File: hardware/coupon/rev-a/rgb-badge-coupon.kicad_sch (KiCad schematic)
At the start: 0 parts

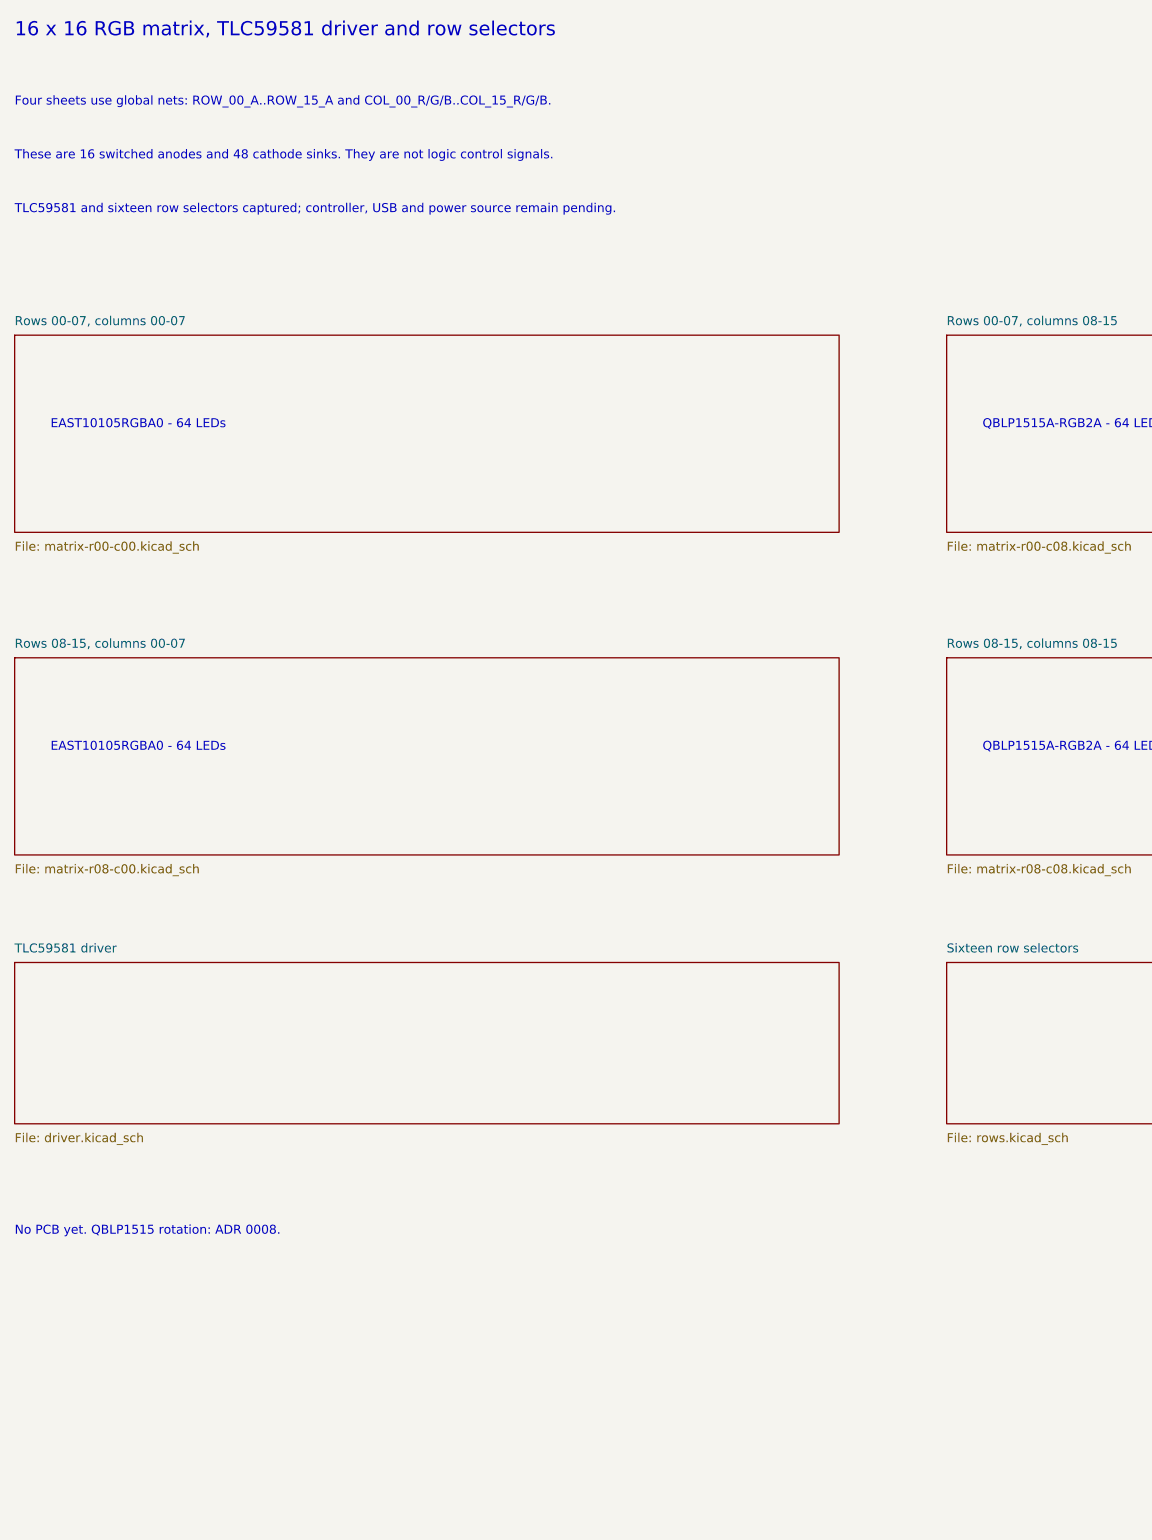
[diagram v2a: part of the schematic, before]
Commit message: Capture Coupon Rev A ESP32-S3 controller
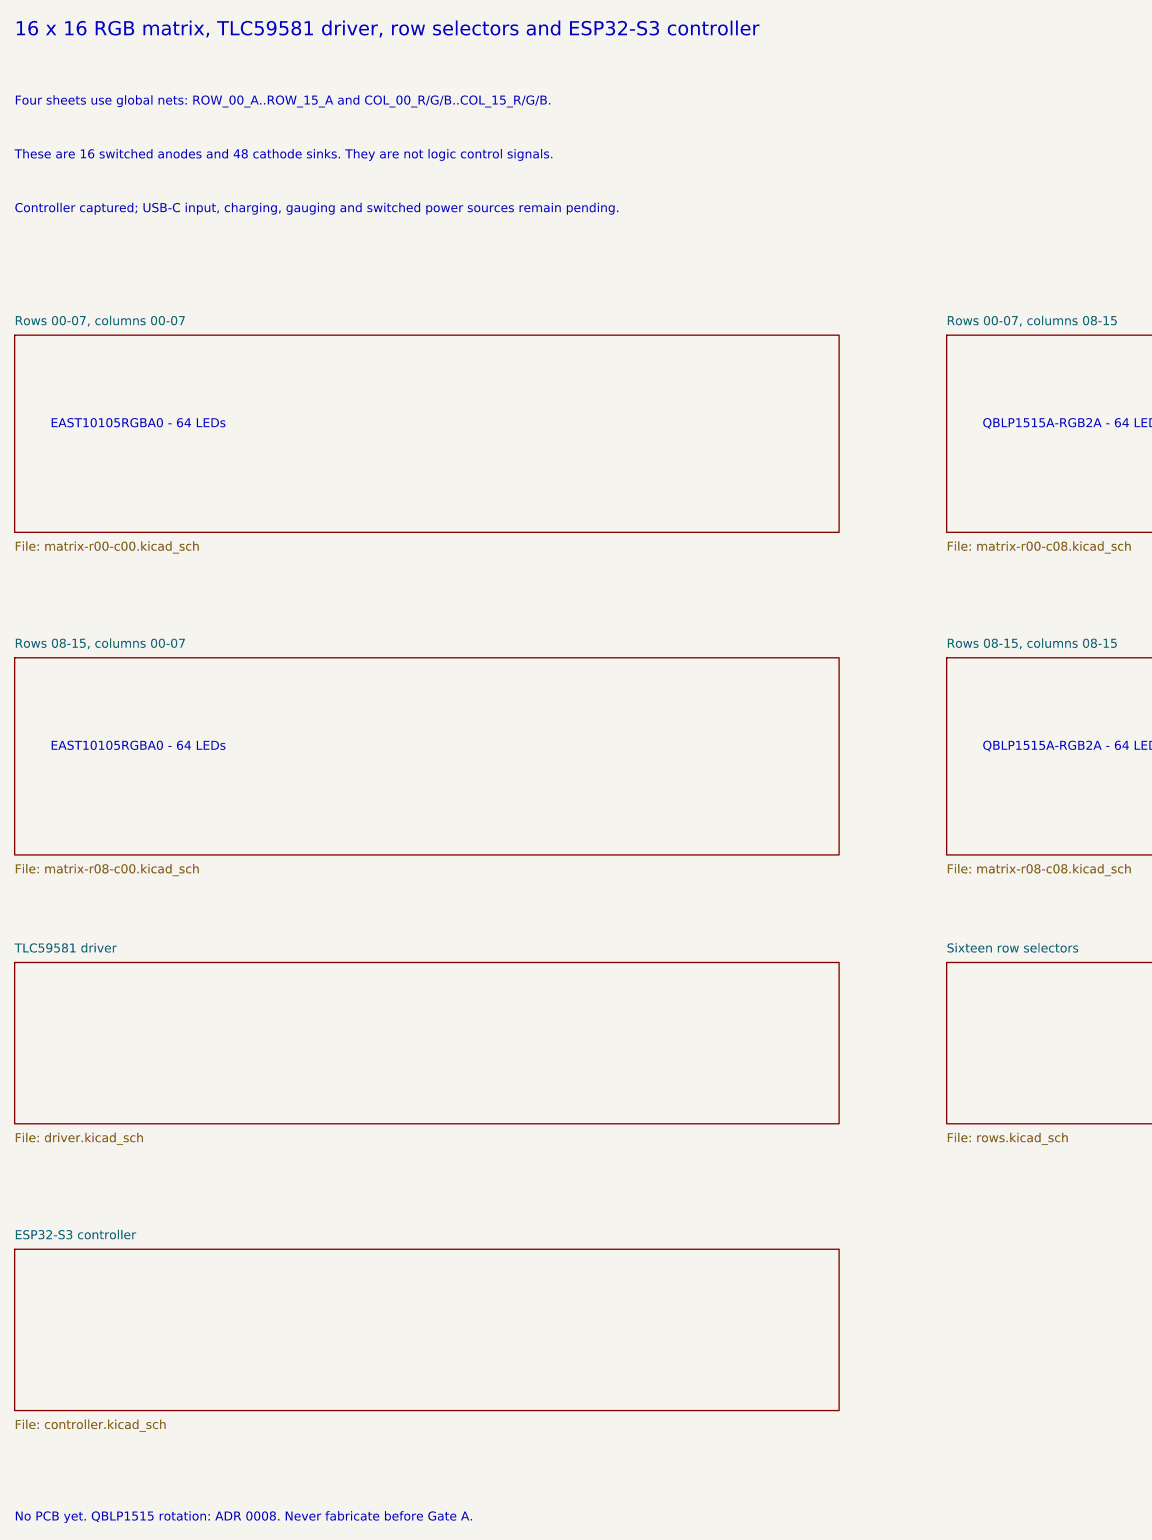
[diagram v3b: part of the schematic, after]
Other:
- added sheet ESP32-S3 controller (controller.kicad_sch)
- note added: "16 x 16 RGB matrix, TLC59581 driver, row selectors and ESP32-S3 controller"
- note added: "Controller captured; USB-C input, charging, gauging and switched power sources remain pending."
- note added: "No PCB yet. QBLP1515 rotation: ADR 0008. Never fabricate before Gate A."
- note removed: "16 x 16 RGB matrix, TLC59581 driver and row selectors"
- note removed: "No PCB yet. QBLP1515 rotation: ADR 0008."
- note removed: "TLC59581 and sixteen row selectors captured; controller, USB and power source remain pending."
- title: Coupon Rev A - matrix, driver and rows -> Coupon Rev A - matrix, driver, rows and controller
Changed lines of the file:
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@@
 (generator "rgb_badge_matrix")
 (generator_version "1.0")
-(paper "A4")
-(title_block (title "Coupon Rev A - matrix, driver and rows") (rev "A-draft") (comment 1 "SPDX-License-Identifier: CERN-OHL-S-2.0") (comment 2 "Controller and power circuits pending"))
-(text "16 x 16 RGB matrix, TLC59581 driver and row selectors" (at 20.32 20.32 0) (effects (font (size 2.0 2.0)) (justify left)))
+(paper "A3")
+(title_block (title "Coupon Rev A - matrix, driver, rows and controller") (rev "A-draft") (comment 1 "SPDX-License-Identifier: CERN-OHL-S-2.0") (comment 2 "USB-C input, charging and switched power circuits pending"))
+(text "16 x 16 RGB matrix, TLC59581 driver, row selectors and ESP32-S3 controller" (at 20.32 20.32 0) (effects (font (size 2.0 2.0)) (justify left)))
 (text "Four sheets use global nets: ROW_00_A..ROW_15_A and COL_00_R/G/B..COL_15_R/G/B." (at 20.32 30.48 0) (effects (font (size 1.27 1.27)) (justify left)))
 (text "These are 16 switched anodes and 48 cathode sinks. They are not logic control signals." (at 20.32 38.10 0) (effects (font (size 1.27 1.27)) (justify left)))
-(text "TLC59581 and sixteen row selectors captured; controller, USB and power source remain pending." (at 20.32 45.72 0) (effects (font (size 1.27 1.27)) (justify left)))
-(text "No PCB yet. QBLP1515 rotation: ADR 0008." (at 20.32 190.50 0) (effects (font (size 1.27 1.27)) (justify left)))
+(text "Controller captured; USB-C input, charging, gauging and switched power sources remain pending." (at 20.32 45.72 0) (effects (font (size 1.27 1.27)) (justify left)))
+(text "No PCB yet. QBLP1515 rotation: ADR 0008. Never fabricate before Gate A." (at 20.32 231.14 0) (effects (font (size 1.27 1.27)) (justify left)))
 (sheet (at 20.32 63.50) (size 116.84 27.94)
 (exclude_from_sim no) (in_bom yes) (on_board yes) (dnp no)
@@
 (property "Sheetfile" "rows.kicad_sch" (at 152.40 176.53 0) (effects (font (size 1.27 1.27)) (justify left top)))
 (instances (project "rgb-badge-coupon" (path "/207fb68e-2ddb-46bb-8712-eba2f8c5eef6" (page "7")))))
+(sheet (at 20.32 193.04) (size 116.84 22.86)
+(exclude_from_sim no) (in_bom yes) (on_board yes) (dnp no)
+(stroke (width 0.1524) (type solid)) (fill (color 0 0 0 0))
+(property "Sheetname" "ESP32-S3 controller" (at 20.32 191.77 0) (effects (font (size 1.27 1.27)) (justify left bottom)))
+(property "Sheetfile" "controller.kicad_sch" (at 20.32 217.17 0) (effects (font (size 1.27 1.27)) (justify left top)))
+(instances (project "rgb-badge-coupon" (path "/207fb68e-2ddb-46bb-8712-eba2f8c5eef6" (page "8")))))
 (sheet_instances (path "/" (page "1")))
 (embedded_fonts no)

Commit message: Capture conditioned USB permission gates and verify their actual wiring
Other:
- added sheet USB input conditioning (staged) (usb-conditioning.kicad_sch)
- added sheet USB permission gates (staged) (usb-permission.kicad_sch)
- note added: "USB logic captured with test boundaries; detectors, startup inhibition, charging and rail sources remain pending."
- note removed: "Controller captured; USB-C input, charging, gauging and switched power sources remain pending."
- title: Coupon Rev A - matrix, driver, rows and controller -> Coupon Rev A - display, controller and staged USB logic
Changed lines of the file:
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@@
 (generator_version "1.0")
 (paper "A3")
-(title_block (title "Coupon Rev A - matrix, driver, rows and controller") (rev "A-draft") (comment 1 "SPDX-License-Identifier: CERN-OHL-S-2.0") (comment 2 "USB-C input, charging and switched power circuits pending"))
+(title_block (title "Coupon Rev A - display, controller and staged USB logic") (rev "A-draft") (comment 1 "SPDX-License-Identifier: CERN-OHL-S-2.0") (comment 2 "USB detectors, supply supervision, charging and switched power pending"))
 (text "16 x 16 RGB matrix, TLC59581 driver, row selectors and ESP32-S3 controller" (at 20.32 20.32 0) (effects (font (size 2.0 2.0)) (justify left)))
 (text "Four sheets use global nets: ROW_00_A..ROW_15_A and COL_00_R/G/B..COL_15_R/G/B." (at 20.32 30.48 0) (effects (font (size 1.27 1.27)) (justify left)))
 (text "These are 16 switched anodes and 48 cathode sinks. They are not logic control signals." (at 20.32 38.10 0) (effects (font (size 1.27 1.27)) (justify left)))
-(text "Controller captured; USB-C input, charging, gauging and switched power sources remain pending." (at 20.32 45.72 0) (effects (font (size 1.27 1.27)) (justify left)))
+(text "USB logic captured with test boundaries; detectors, startup inhibition, charging and rail sources remain pending." (at 20.32 45.72 0) (effects (font (size 1.27 1.27)) (justify left)))
 (text "No PCB yet. QBLP1515 rotation: ADR 0008. Never fabricate before Gate A." (at 20.32 231.14 0) (effects (font (size 1.27 1.27)) (justify left)))
 (sheet (at 20.32 63.50) (size 116.84 27.94)
@@
 (property "Sheetfile" "controller.kicad_sch" (at 20.32 217.17 0) (effects (font (size 1.27 1.27)) (justify left top)))
 (instances (project "rgb-badge-coupon" (path "/207fb68e-2ddb-46bb-8712-eba2f8c5eef6" (page "8")))))
+(sheet (at 152.40 193.04) (size 116.84 22.86)
+(exclude_from_sim no) (in_bom yes) (on_board yes) (dnp no)
+(stroke (width 0.1524) (type solid)) (fill (color 0 0 0 0))
+(property "Sheetname" "USB input conditioning (staged)" (at 152.40 191.77 0) (effects (font (size 1.27 1.27)) (justify left bottom)))
+(property "Sheetfile" "usb-conditioning.kicad_sch" (at 152.40 217.17 0) (effects (font (size 1.27 1.27)) (justify left top)))
+(instances (project "rgb-badge-coupon" (path "/207fb68e-2ddb-46bb-8712-eba2f8c5eef6" (page "9")))))
+(sheet (at 284.48 193.04) (size 116.84 22.86)
+(exclude_from_sim no) (in_bom yes) (on_board yes) (dnp no)
+(stroke (width 0.1524) (type solid)) (fill (color 0 0 0 0))
+(property "Sheetname" "USB permission gates (staged)" (at 284.48 191.77 0) (effects (font (size 1.27 1.27)) (justify left bottom)))
+(property "Sheetfile" "usb-permission.kicad_sch" (at 284.48 217.17 0) (effects (font (size 1.27 1.27)) (justify left top)))
+(instances (project "rgb-badge-coupon" (path "/207fb68e-2ddb-46bb-8712-eba2f8c5eef6" (page "10")))))
 (sheet_instances (path "/" (page "1")))
 (embedded_fonts no)

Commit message: Capture USB detection and switched data path after native logic review
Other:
- added sheet USB interface (staged input) (usb-interface.kicad_sch)
- note added: "USB data/detectors/logic captured; input protection, startup inhibition, charging and switched rails remain pending."
- note removed: "USB logic captured with test boundaries; detectors, startup inhibition, charging and rail sources remain pending."
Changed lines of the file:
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@@
 (generator_version "1.0")
 (paper "A3")
-(title_block (title "Coupon Rev A - display, controller and staged USB logic") (rev "A-draft") (comment 1 "SPDX-License-Identifier: CERN-OHL-S-2.0") (comment 2 "USB detectors, supply supervision, charging and switched power pending"))
+(title_block (title "Coupon Rev A - display, controller and staged USB logic") (rev "A-draft") (comment 1 "SPDX-License-Identifier: CERN-OHL-S-2.0") (comment 2 "Input protection, supervision, charging and switched power pending"))
 (text "16 x 16 RGB matrix, TLC59581 driver, row selectors and ESP32-S3 controller" (at 20.32 20.32 0) (effects (font (size 2.0 2.0)) (justify left)))
 (text "Four sheets use global nets: ROW_00_A..ROW_15_A and COL_00_R/G/B..COL_15_R/G/B." (at 20.32 30.48 0) (effects (font (size 1.27 1.27)) (justify left)))
 (text "These are 16 switched anodes and 48 cathode sinks. They are not logic control signals." (at 20.32 38.10 0) (effects (font (size 1.27 1.27)) (justify left)))
-(text "USB logic captured with test boundaries; detectors, startup inhibition, charging and rail sources remain pending." (at 20.32 45.72 0) (effects (font (size 1.27 1.27)) (justify left)))
+(text "USB data/detectors/logic captured; input protection, startup inhibition, charging and switched rails remain pending." (at 20.32 45.72 0) (effects (font (size 1.27 1.27)) (justify left)))
 (text "No PCB yet. QBLP1515 rotation: ADR 0008. Never fabricate before Gate A." (at 20.32 231.14 0) (effects (font (size 1.27 1.27)) (justify left)))
 (sheet (at 20.32 63.50) (size 116.84 27.94)
@@
 (property "Sheetfile" "usb-permission.kicad_sch" (at 284.48 217.17 0) (effects (font (size 1.27 1.27)) (justify left top)))
 (instances (project "rgb-badge-coupon" (path "/207fb68e-2ddb-46bb-8712-eba2f8c5eef6" (page "10")))))
+(sheet (at 284.48 152.40) (size 116.84 22.86)
+(exclude_from_sim no) (in_bom yes) (on_board yes) (dnp no)
+(stroke (width 0.1524) (type solid)) (fill (color 0 0 0 0))
+(property "Sheetname" "USB interface (staged input)" (at 284.48 151.13 0) (effects (font (size 1.27 1.27)) (justify left bottom)))
+(property "Sheetfile" "usb-interface.kicad_sch" (at 284.48 176.53 0) (effects (font (size 1.27 1.27)) (justify left top)))
+(instances (project "rgb-badge-coupon" (path "/207fb68e-2ddb-46bb-8712-eba2f8c5eef6" (page "11")))))
 (sheet_instances (path "/" (page "1")))
 (embedded_fonts no)

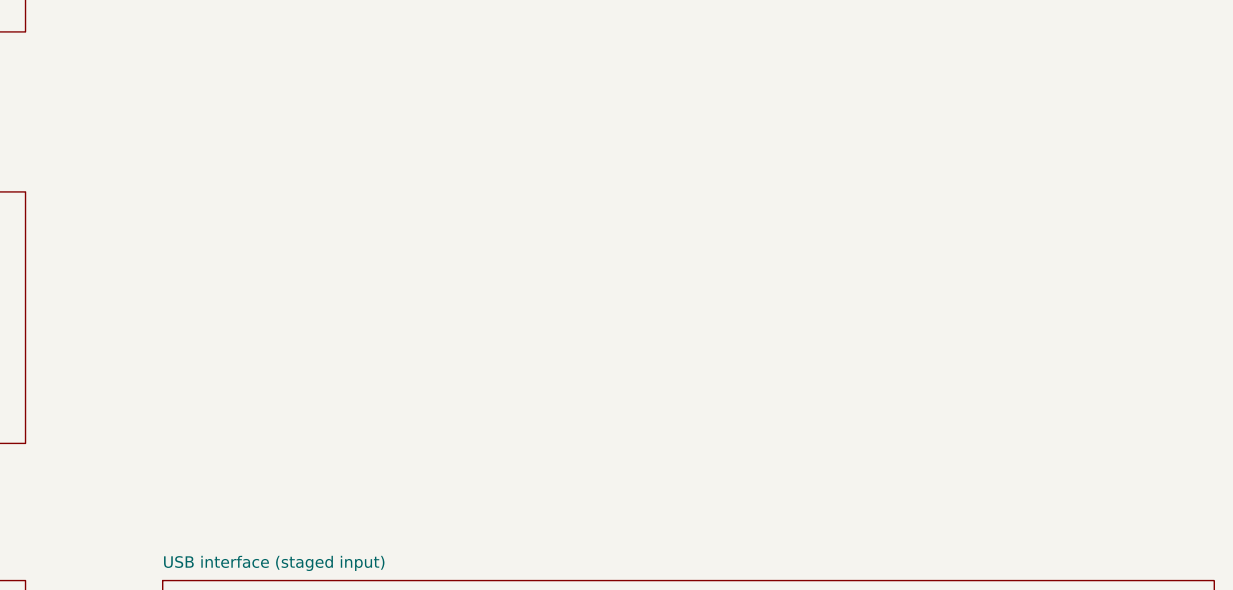
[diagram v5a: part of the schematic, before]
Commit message: Stage switched MAX17048 gauge and audited pull-ups
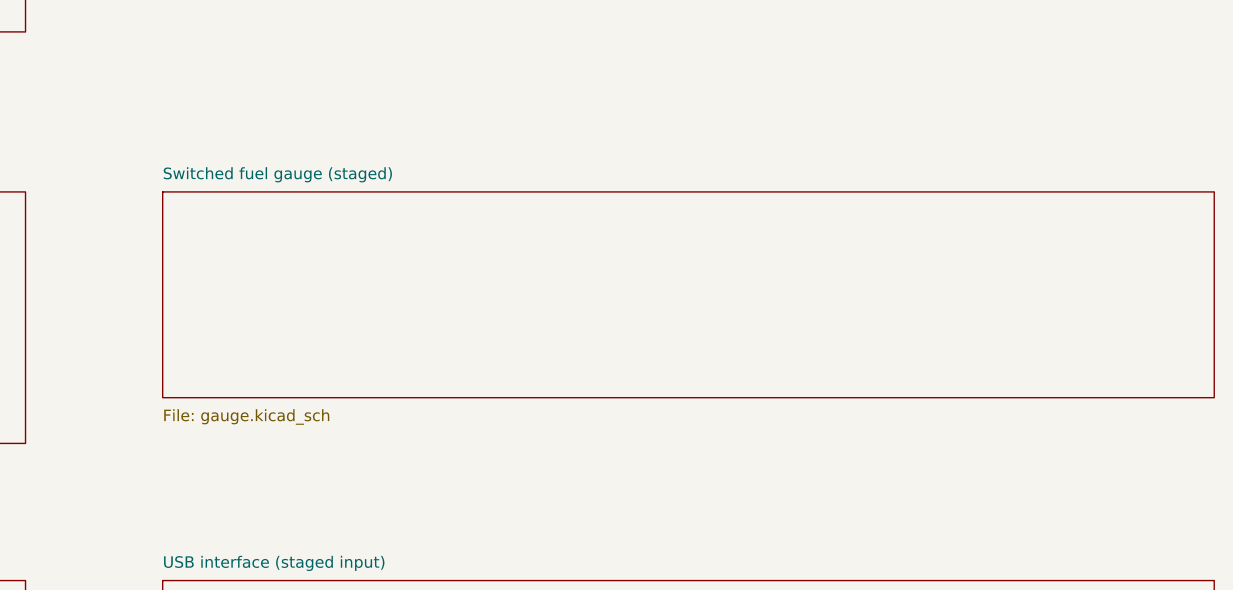
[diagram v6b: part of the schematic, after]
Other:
- added sheet Switched fuel gauge (staged) (gauge.kicad_sch)
- title: Coupon Rev A - display, controller and staged USB logic -> Coupon Rev A - display, controller, USB logic and staged gauge
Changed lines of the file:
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@@
 (generator_version "1.0")
 (paper "A3")
-(title_block (title "Coupon Rev A - display, controller and staged USB logic") (rev "A-draft") (comment 1 "SPDX-License-Identifier: CERN-OHL-S-2.0") (comment 2 "Input protection, supervision, charging and switched power pending"))
+(title_block (title "Coupon Rev A - display, controller, USB logic and staged gauge") (rev "A-draft") (comment 1 "SPDX-License-Identifier: CERN-OHL-S-2.0") (comment 2 "Input protection, charging, gauge switch and switched power pending"))
 (text "16 x 16 RGB matrix, TLC59581 driver, row selectors and ESP32-S3 controller" (at 20.32 20.32 0) (effects (font (size 2.0 2.0)) (justify left)))
 (text "Four sheets use global nets: ROW_00_A..ROW_15_A and COL_00_R/G/B..COL_15_R/G/B." (at 20.32 30.48 0) (effects (font (size 1.27 1.27)) (justify left)))
@@
 (property "Sheetfile" "usb-interface.kicad_sch" (at 284.48 176.53 0) (effects (font (size 1.27 1.27)) (justify left top)))
 (instances (project "rgb-badge-coupon" (path "/207fb68e-2ddb-46bb-8712-eba2f8c5eef6" (page "11")))))
+(sheet (at 284.48 109.22) (size 116.84 22.86)
+(exclude_from_sim no) (in_bom yes) (on_board yes) (dnp no)
+(stroke (width 0.1524) (type solid)) (fill (color 0 0 0 0))
+(property "Sheetname" "Switched fuel gauge (staged)" (at 284.48 107.95 0) (effects (font (size 1.27 1.27)) (justify left bottom)))
+(property "Sheetfile" "gauge.kicad_sch" (at 284.48 133.35 0) (effects (font (size 1.27 1.27)) (justify left top)))
+(instances (project "rgb-badge-coupon" (path "/207fb68e-2ddb-46bb-8712-eba2f8c5eef6" (page "12")))))
 (sheet_instances (path "/" (page "1")))
 (embedded_fonts no)
